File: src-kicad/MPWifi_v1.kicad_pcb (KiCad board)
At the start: 2 copper layers, 16 parts, among them CON1 Micro_SD_Card, M1 ESP8266-12E, P1 CONN_01X04, P2 Flash, Q1 BSS138, Q2 BSS138, U1 MCP1703T-3302E/CB

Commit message: Board v1.0 and BOM
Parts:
- P2: footprint Pin_Headers:Pin_Header_Angled_1x03 -> Pin_Headers:Pin_Header_Straight_1x03
- moved CON1 21.5 mm to (149.0, 80.9), turned to 270 degrees
- moved P2 16.1 mm to (150.7, 70.1), turned to 180 degrees
- moved R6 6.62 mm to (166.8, 73.1), turned to 270 degrees
- moved C1 1.65 mm to (166.8, 70.0)
- moved Q1 1.65 mm to (161.8, 69.3)
- moved C2 1.65 mm to (166.8, 66.9)
- moved R3 1.65 mm to (158.8, 65.9)
- moved D1 1.65 mm to (155.1, 69.0)
- moved Q2 1.65 mm to (158.1, 69.3)
- moved R1 1.65 mm to (155.1, 65.8)
- moved P1 1.65 mm to (163.2, 62.5)
- moved R2 1.65 mm to (162.9, 65.9)
- moved R4 1.65 mm to (161.5, 72.7)
- moved R5 1.65 mm to (158.1, 72.7)
- moved U1 1.65 mm to (164.2, 68.4)
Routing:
- net GND: track 21.2 -> 149.9 mm, vias 0 -> 2
- net Net-(M1-Pad16): track 2.44 -> 30.1 mm, vias 0 -> 1
- net /DETECT_SWITCH: track 0.00 -> 21.6 mm, vias 0 -> 1
- net Net-(M1-Pad15): track 2.48 -> 23.1 mm, vias 0 -> 1
- net Net-(M1-Pad12): track 0.00 -> 20.3 mm
- net +3V3: track 38.3 -> 58.5 mm, vias 0 -> 2
- net /MOSI: track 28.0 -> 13.8 mm
- net /MISO: track 15.5 -> 25.1 mm
- net /CS: track 19.0 -> 14.0 mm
- net /TX: track 6.48 -> 8.59 mm
- net VCC: track 46.3 -> 48.2 mm
- net /SCLK: track 19.9 -> 18.5 mm
- added copper zone on B.Cu, net GND
- added copper zone on F.Cu, net GND
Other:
- board outline added: 24.1 x 44 mm
- net class Default: clearance 0.2 -> 0.1492
- rule trace_clearance: 0.2 -> 0.1492
- board text added: "MPWifi v1.0 M Prime nov 2016"

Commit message: v1.0 PCB
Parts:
- moved P1 2.28 mm to (162.8, 60.2)
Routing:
- net VCC: track 48.2 -> 53.1 mm
- net GND: track 149.9 -> 152.4 mm
- net /TX: track 8.59 -> 10.7 mm
- net /RX: track 7.49 -> 9.62 mm
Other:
- board size 24.1 x 44 mm -> 24.1 x 45.9 mm
- board text added: "GND"
- board text added: "M Prime v1.0"
- board text added: "PWR"
- board text added: "Rx"
- board text added: "Tx"
- board text added: "Vcc"
- board text removed: "MPWifi v1.0 M Prime nov 2016"

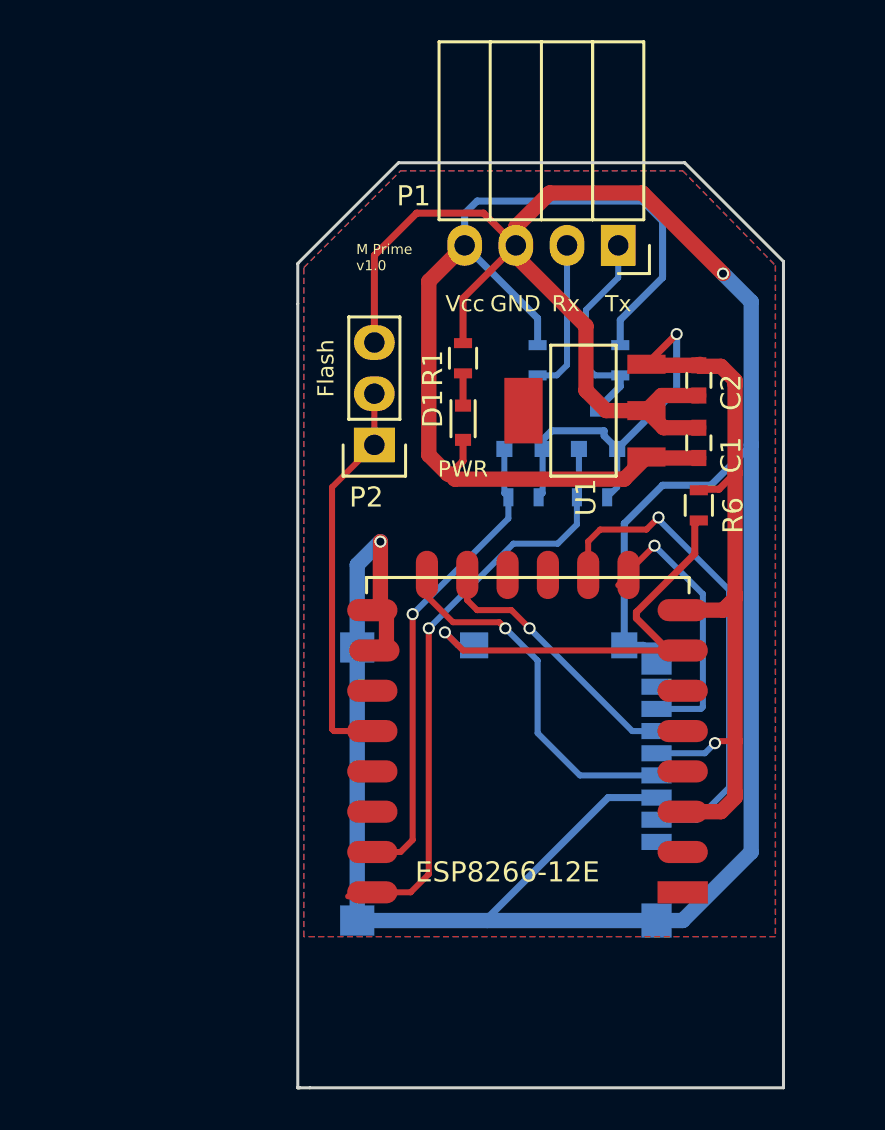
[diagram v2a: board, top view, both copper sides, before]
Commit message: microSD footprint & retrack
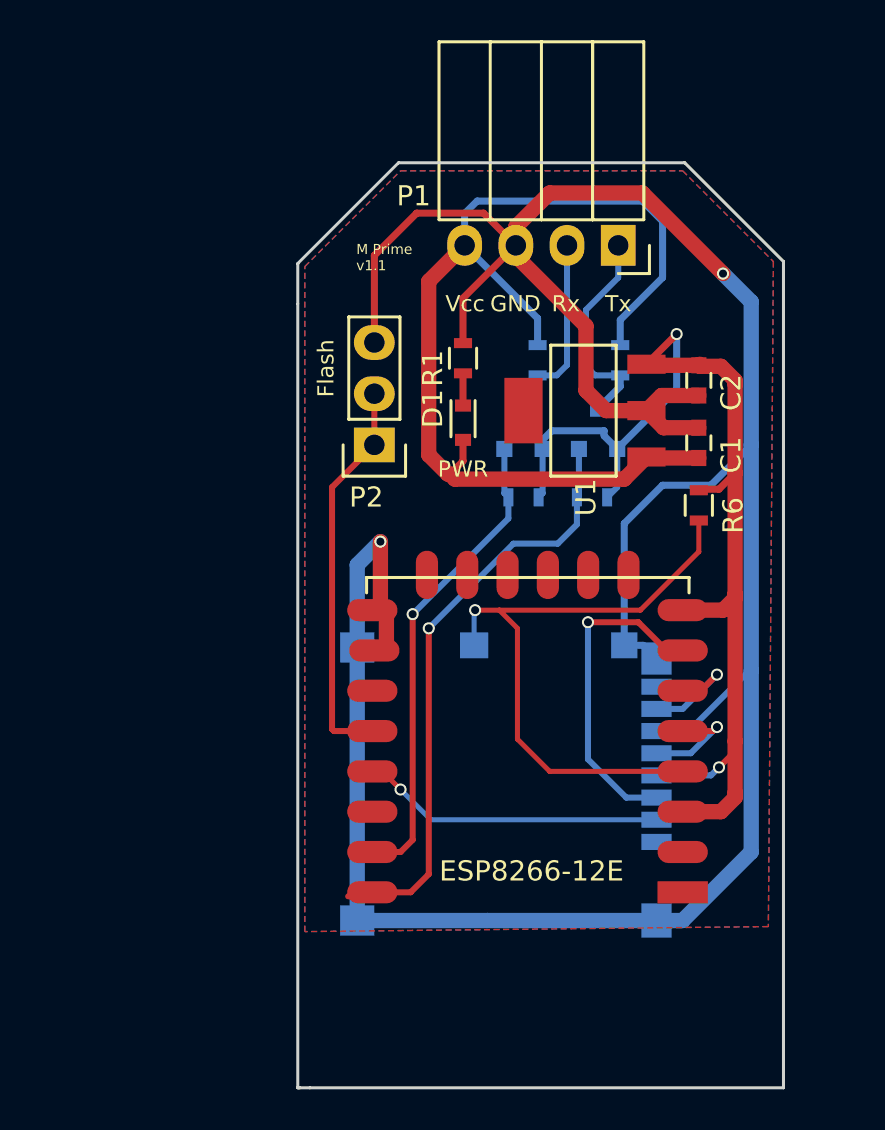
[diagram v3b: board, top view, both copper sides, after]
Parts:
- renumbered CON1 to uSD
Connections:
- M1 pad 1: Net-(M1-Pad1) -> (no net)
- M1 pad 11: Net-(M1-Pad11) -> (no net)
- M1 pad 13: Net-(M1-Pad13) -> /CS
- M1 pad 14: Net-(M1-Pad14) -> (no net)
- M1 pad 17: /CS -> (no net)
- M1 pad 18: /MISO -> (no net)
- M1 pad 19: Net-(M1-Pad19) -> (no net)
- M1 pad 2: Net-(M1-Pad2) -> (no net)
- M1 pad 20: Net-(M1-Pad20) -> (no net)
- M1 pad 21: /MOSI -> (no net)
- M1 pad 22: /SCLK -> (no net)
- M1 pad 4: Net-(M1-Pad4) -> /DETECT_SWITCH
- M1 pad 5: Net-(M1-Pad5) -> /SCLK
- M1 pad 6: Net-(M1-Pad6) -> /MISO
- M1 pad 7: /DETECT_SWITCH -> /MOSI
- uSD pad 1: Net-(CON1-Pad1) -> (no net)
- uSD pad 8: Net-(CON1-Pad8) -> (no net)
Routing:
- net /MISO: track 25.1 -> 6.44 mm
- net /SCLK: track 18.5 -> 6.02 mm
- net /DETECT_SWITCH: track 21.6 -> 31.0 mm
- net GND: track 152.4 -> 147.2 mm
- net (no net): track 0.00 -> 2.22 mm
- net /MOSI: track 13.8 -> 15.6 mm
- net +3V3: track 58.5 -> 59.3 mm
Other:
- board text added: "M Prime v1.1"
- board text removed: "M Prime v1.0"
